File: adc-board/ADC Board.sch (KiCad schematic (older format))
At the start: 113 parts, among them J1 ST-LINK/V2, J2 Sensors, J3 USART1, J4 USART6, J5 UE27AC5410H, U1 STM32H743ZITx, U10 MCP1501T-30E/SN, U11 AP7361C-33E-13, U12 AP7361C-33E-13, U13 P78E05-1000, U3 USBLC6-2SC6, U4 AD8544, U5 AD8544, U6 AD8544, U7 AD8544, U8 AD8544, U9 AD8544, Y1 NX3225GD-8.000M-EXS00A-CG04874

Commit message: adc board schematic tweaks and complete relayout
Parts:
- removed C18, C19: 1uF, Capacitors_SMD:C_0805_HandSoldering, symbol Device:C_Small
- removed C22, C23, C24, C25: 4.7uF, Capacitors_SMD:C_0805_HandSoldering, symbol Device:C_Small
- removed C31: DC32, Capacitors_SMD:C_0805, symbol Device:C
- removed J2: Sensors, Pin_Headers:Pin_Header_Angled_2x22_Pitch2.54mm, symbol Connector_Generic:Conn_02x22_Odd_Even
- removed R1, R10, R11, R12, R13, R14, R15, R16, R17, R18, R19, R2, R20, R21, R22, R3, R4, R5, R6, R7, R8, R9: 2200, Resistors_SMD:R_0805_HandSoldering, symbol Device:R_Small_US
- removed TP1, TP10, TP11, TP12, TP13, TP14, TP15, TP16, TP17, TP18, TP19, TP2, TP20, TP21, TP22, TP3, TP4, TP5, TP6, TP7, TP8, TP9: TestPoint, Pin_Headers:Pin_Header_Straight_1x01_Pitch1.00mm, symbol Connector:TestPoint
- removed U11, U12: AP7361C-33E-13, TO_SOT_Packages_SMD:SOT-223-3_TabPin2, symbol Regulator_Linear:AP7361C-33E
- removed U4, U5, U6, U7, U8, U9: AD8544, SMD_Packages:SSOP-14, symbol AD8544:AD8544
- added C55, C56: DC, Capacitors_SMD:C_0805, symbol Device:C_Small
- C33: renamed from C16; footprint Capacitors_SMD:C_0805_HandSoldering -> Capacitors_SMD:C_0805
- C34: renamed from C3; footprint Capacitors_SMD:C_0805_HandSoldering -> Capacitors_SMD:C_0805
- C35: renamed from C4; footprint Capacitors_SMD:C_0805_HandSoldering -> Capacitors_SMD:C_0805
- C36: renamed from C5; footprint Capacitors_SMD:C_0805_HandSoldering -> Capacitors_SMD:C_0805
- C37: renamed from C6; footprint Capacitors_SMD:C_0805_HandSoldering -> Capacitors_SMD:C_0805
- C38: renamed from C7; footprint Capacitors_SMD:C_0805_HandSoldering -> Capacitors_SMD:C_0805
- C39: renamed from C8; footprint Capacitors_SMD:C_0805_HandSoldering -> Capacitors_SMD:C_0805
- C40: renamed from C9; footprint Capacitors_SMD:C_0805_HandSoldering -> Capacitors_SMD:C_0805
- C41: renamed from C10; footprint Capacitors_SMD:C_0805_HandSoldering -> Capacitors_SMD:C_0805
- C42: renamed from C11; footprint Capacitors_SMD:C_0805_HandSoldering -> Capacitors_SMD:C_0805
- C43: renamed from C12; footprint Capacitors_SMD:C_0805_HandSoldering -> Capacitors_SMD:C_0805
- C44: renamed from C13; footprint Capacitors_SMD:C_0805_HandSoldering -> Capacitors_SMD:C_0805
- C45: renamed from C14; footprint Capacitors_SMD:C_0805_HandSoldering -> Capacitors_SMD:C_0805
- C46: renamed from C15; footprint Capacitors_SMD:C_0805_HandSoldering -> Capacitors_SMD:C_0805
- C47: renamed from C1; footprint Capacitors_SMD:C_0805_HandSoldering -> Capacitors_SMD:C_0805
- C48: renamed from C2; footprint Capacitors_SMD:C_0805_HandSoldering -> Capacitors_SMD:C_0805
- C49: renamed from C29; footprint Capacitors_SMD:C_0805_HandSoldering -> Capacitors_SMD:C_0805
- C50: renamed from C30; footprint Capacitors_SMD:C_0805_HandSoldering -> Capacitors_SMD:C_0805
- C51: renamed from C20; footprint Capacitors_SMD:C_0805_HandSoldering -> Capacitors_SMD:C_0805
- C52: renamed from C21; footprint Capacitors_SMD:C_0805_HandSoldering -> Capacitors_SMD:C_0805
- R30: renamed from R29; footprint Resistors_SMD:R_0805_HandSoldering -> Resistors_SMD:R_0805
- R31: renamed from R23; footprint Resistors_SMD:R_0805_HandSoldering -> Resistors_SMD:R_0805
- R55: renamed from R25; footprint Resistors_SMD:R_0805_HandSoldering -> Resistors_SMD:R_0805
- R56: renamed from R26; footprint Resistors_SMD:R_0805_HandSoldering -> Resistors_SMD:R_0805
- R57: renamed from R27; footprint Resistors_SMD:R_0805_HandSoldering -> Resistors_SMD:R_0805
- R58: renamed from R28; footprint Resistors_SMD:R_0805_HandSoldering -> Resistors_SMD:R_0805
- U13: value P78E05-1000 -> 3.3V Reg
- renumbered C17 to C32, C26 to C53, C27 to C54, J1 to J2, U1 to U0, U3 to U9
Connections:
- net labels removed: +12V, ETH_TXD0, ETH_TXD1, ETH_TX_EN, Sen10R, Sen11R, Sen12R, Sen13R, Sen14R, Sen15R, Sen16R, Sen17R, Sen18R, Sen19R, Sen1R, Sen20R, Sen21R, Sen22R, Sen2R, Sen3R, Sen4R, Sen5R, Sen6R, Sen7R, Sen8R, Sen9R
- wire segments 487 -> 297
- no-connect marks 71 -> 76
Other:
- note removed: "Op amps taking the "raw" voltage off the sense\nresistors, and buffering it for the ADCs. Also protects\nthe ADC inputs. Op amp output voltage is limited to\nVDDA, and they're cheap/easy to replace if damaged."
- note removed: "Separate linear regulators for Digital and Analog"
- moved on the sheet: C47, C48, C49, C50, H1, H2, H3, H4, R30, TP23, TP24, TP25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

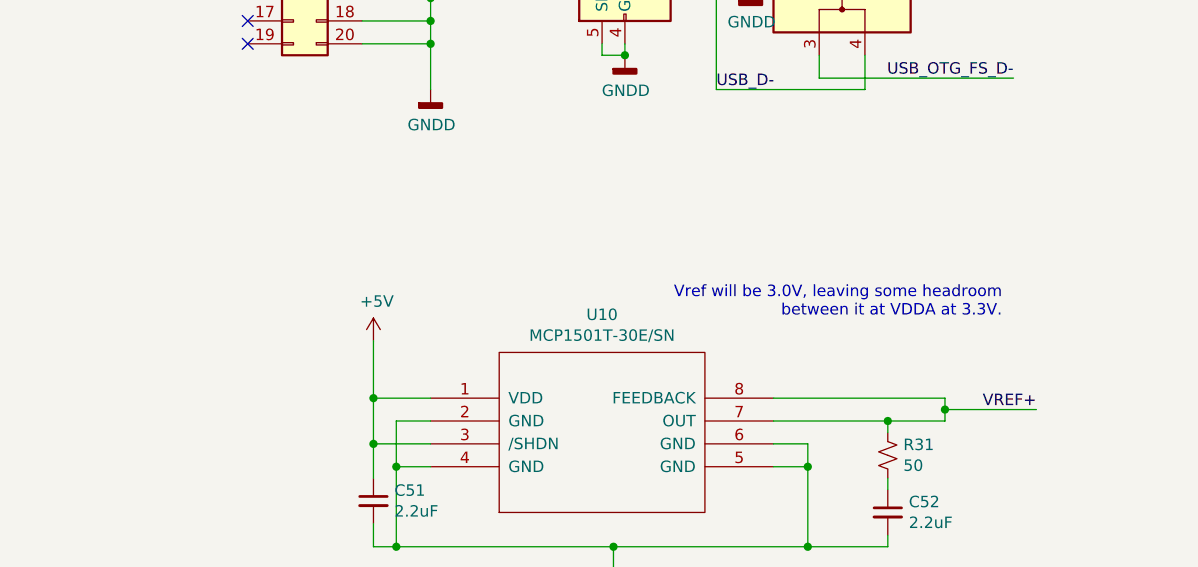
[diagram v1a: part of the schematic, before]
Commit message: correct RS485 termination resistors, adjust ground pours
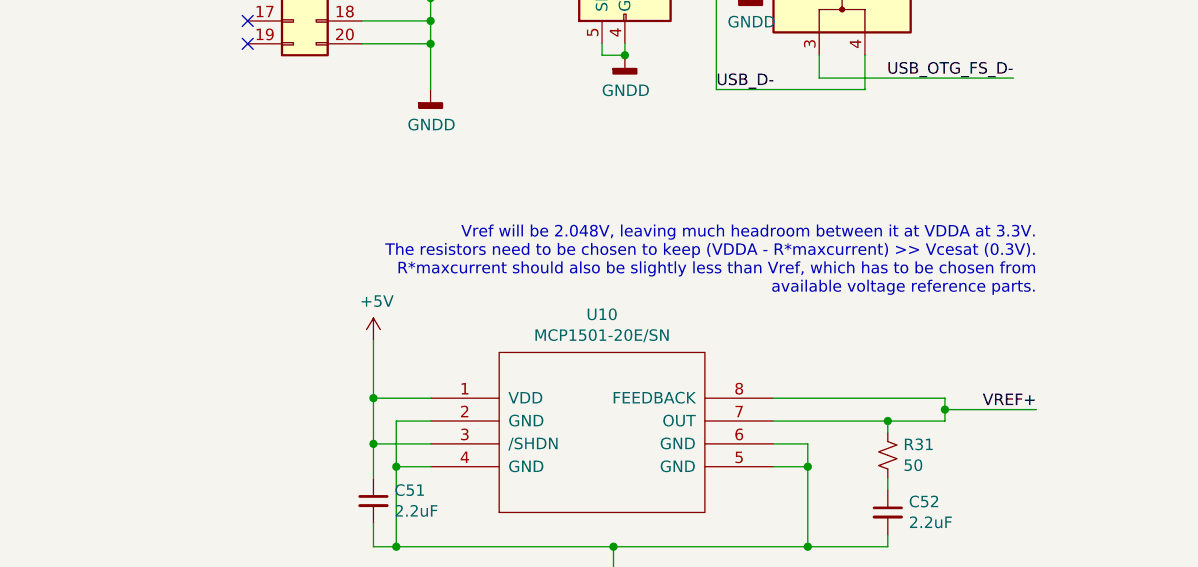
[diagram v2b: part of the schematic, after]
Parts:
- U10: value MCP1501T-30E/SN -> MCP1501-20E/SN
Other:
- note added: "Vref will be 2.048V, leaving much headroom between it at VDDA at 3.3V.\nThe resistors need to be chosen to keep (VDDA - R*maxcurrent) >> Vcesat (0.3V).\nR*maxcurrent should also be slightly less than Vref, which has to be chosen from\navailable voltage reference parts."
- note removed: "Vref will be 3.0V, leaving some headroom\nbetween it at VDDA at 3.3V."
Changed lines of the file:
@@
 P 12400 7400
 F 0 "U10" H 12400 7915 50  0000 C CNN
-F 1 "MCP1501T-30E/SN" H 12400 7824 50  0000 C CNN
+F 1 "MCP1501-20E/SN" H 12400 7824 50  0000 C CNN
 F 2 "SMD_Packages:SOIC-8-N" H 12400 7400 50  0001 C CNN
 F 3 "DOCUMENTATION" H 12400 7400 50  0001 C CNN
@@
 	1    0    0    -1
 $EndComp
-Text Notes 14150 6900 2    50   ~ 0
-Vref will be 3.0V, leaving some headroom\nbetween it at VDDA at 3.3V.
+Text Notes 14300 6800 2    50   ~ 0
+Vref will be 2.048V, leaving much headroom between it at VDDA at 3.3V.\nThe resistors need to be chosen to keep (VDDA - R*maxcurrent) >> Vcesat (0.3V).\nR*maxcurrent should also be slightly less than Vref, which has to be chosen from\navailable voltage reference parts.
 Text Notes 3600 10550 0    79   ~ 0
 Reference STMicroelectronics Application Note AN4938\nfor details on basic STMH74x circuits

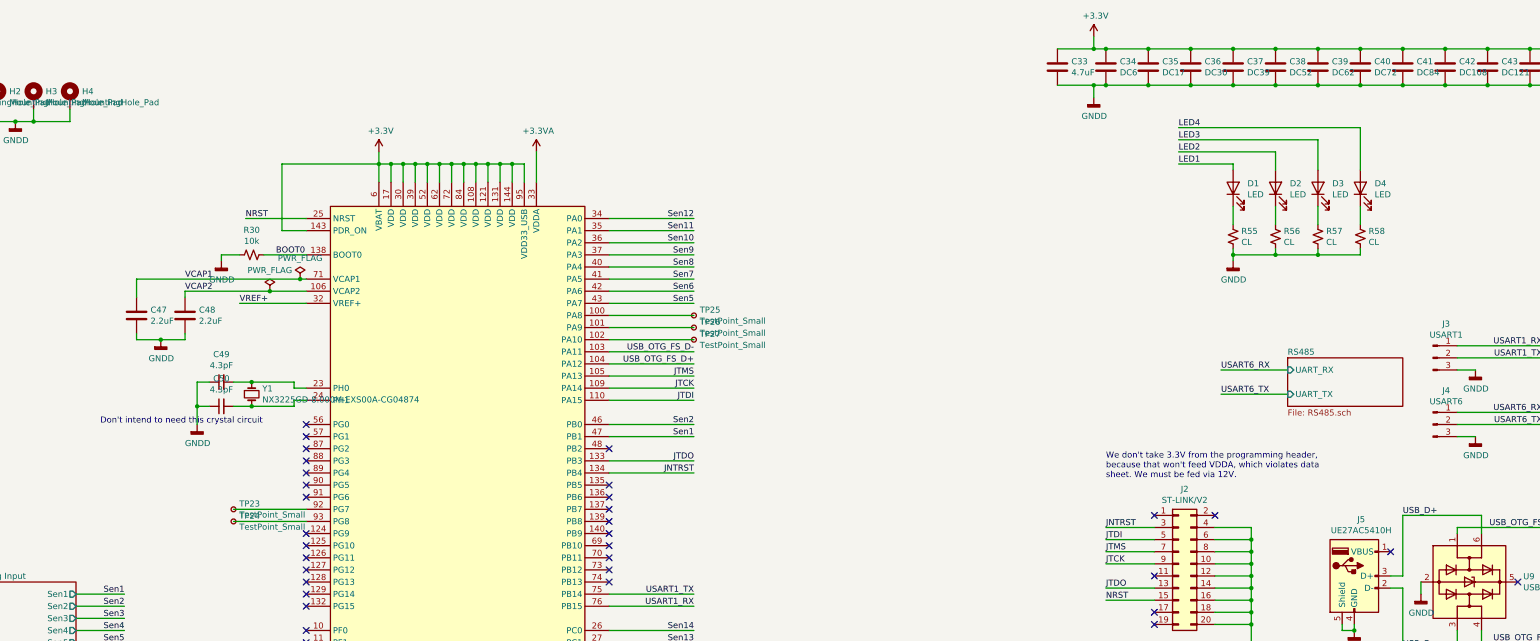
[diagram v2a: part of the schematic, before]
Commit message: alternative power inputs; cap on NRST; 3.3V reg thermal work on PCB
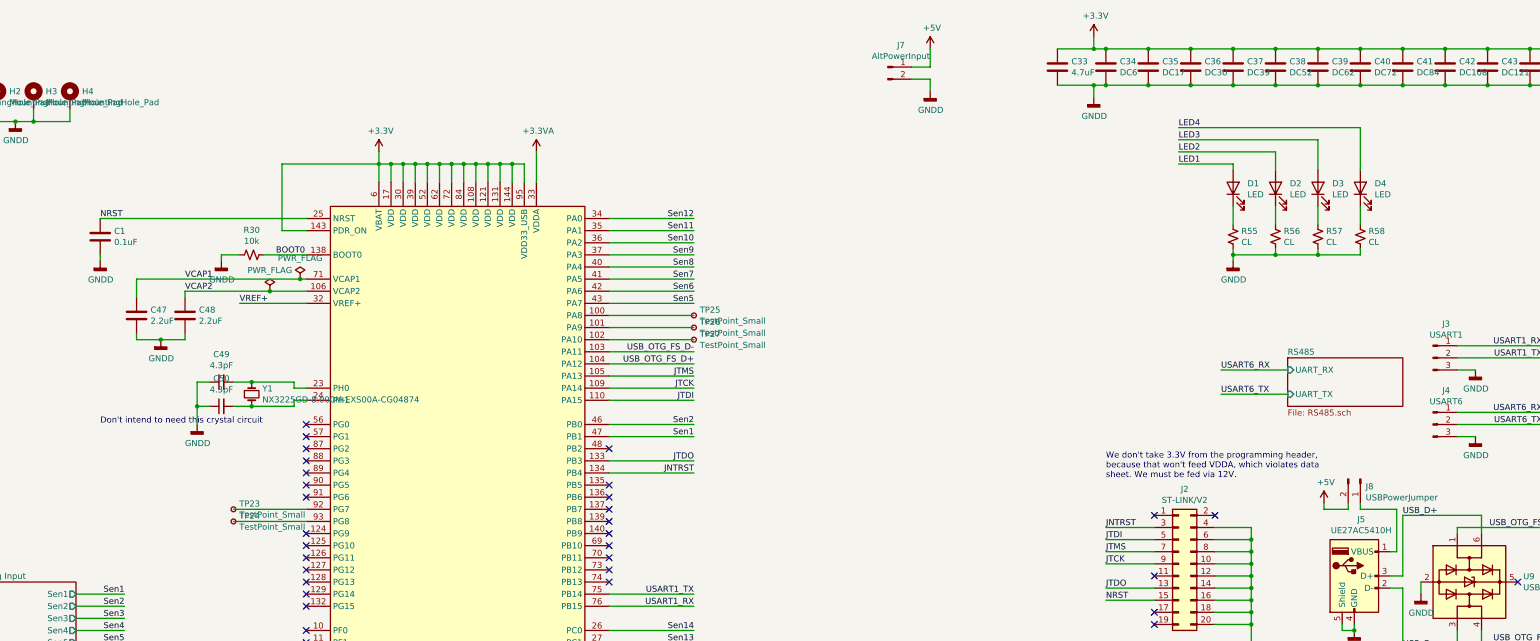
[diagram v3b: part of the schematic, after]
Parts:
- added C1: 0.1uF, Capacitors_SMD:C_0805, symbol Device:C
- added J7: AltPowerInput, Pin_Headers:Pin_Header_Straight_1x02_Pitch2.54mm, symbol Connector:Conn_01x02_Male
- added J8: USBPowerJumper, Pin_Headers:Pin_Header_Straight_1x02_Pitch2.54mm, symbol Connector:Conn_01x02_Male
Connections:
- net +5V: now also J7.1 (Pin_1), J8.2 (Pin_2)
- net GNDD: now also C1.2, J7.2 (Pin_2)
- net NRST: now also C1.1
- net at J5.1 (VBUS): now also J8.1 (Pin_1)
- no-connect marks 76 -> 75
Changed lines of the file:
@@
 NRST
 Wire Wire Line
-	3850 2350 3350 2350
-Text Label 3350 2350 0    50   ~ 0
+	3850 2350 2150 2350
+Text Label 2150 2350 0    50   ~ 0
 NRST
 Wire Wire Line
@@
 	1    0    0    -1
 $EndComp
-NoConn ~ 12800 5100
 Wire Wire Line
 	1450 1550 1600 1550
@@
 	14200 9050 14100 9050
 Connection ~ 14100 9050
+$Comp
+L Connector:Conn_01x02_Male J7
+U 1 1 5FBE56DB
+P 8650 1100
+F 0 "J7" H 8758 1281 50  0000 C CNN
+F 1 "AltPowerInput" H 8758 1190 50  0000 C CNN
+F 2 "Pin_Headers:Pin_Header_Straight_1x02_Pitch2.54mm" H 8650 1100 50  0001 C CNN
+F 3 "~" H 8650 1100 50  0001 C CNN
+	1    8650 1100
+	1    0    0    -1
+$EndComp
+$Comp
+L power:+5V #PWR0135
+U 1 1 5FBE63A7
+P 9000 950
+F 0 "#PWR0135" H 9000 800 50  0001 C CNN
+F 1 "+5V" H 9015 1123 50  0000 C CNN
+F 2 "" H 9000 950 50  0001 C CNN
+F 3 "" H 9000 950 50  0001 C CNN
+	1    9000 950
+	1    0    0    -1
+$EndComp
+Wire Wire Line
+	9000 950  9000 1100
+Wire Wire Line
+	9000 1100 8850 1100
+Wire Wire Line
+	8850 1200 9000 1200
+Wire Wire Line
+	9000 1200 9000 1300
+$Comp
+L power:GNDD #PWR0136
+U 1 1 5FC205C9
+P 9000 1300
+F 0 "#PWR0136" H 9000 1050 50  0001 C CNN
+F 1 "GNDD" H 9004 1145 50  0000 C CNN
+F 2 "" H 9000 1300 50  0001 C CNN
+F 3 "" H 9000 1300 50  0001 C CNN
+	1    9000 1300
+	1    0    0    -1
+$EndComp
+$Comp
+L Connector:Conn_01x02_Male J8
+U 1 1 5FC44C17
+P 12550 4500
+F 0 "J8" V 12612 4544 50  0000 L CNN
+F 1 "USBPowerJumper" V 12703 4544 50  0000 L CNN
+F 2 "Pin_Headers:Pin_Header_Straight_1x02_Pitch2.54mm" H 12550 4500 50  0001 C CNN
+F 3 "~" H 12550 4500 50  0001 C CNN
+	1    12550 4500
+	0    1    1    0
+$EndComp
+Wire Wire Line
+	12800 5100 12850 5100
+Wire Wire Line
+	12850 5100 12850 4750
+Wire Wire Line
+	12850 4750 12550 4750
+Wire Wire Line
+	12550 4750 12550 4700
+Wire Wire Line
+	12450 4700 12450 4750
+$Comp
+L power:+5V #PWR0143
+U 1 1 5FC885B1
+P 12250 4700
+F 0 "#PWR0143" H 12250 4550 50  0001 C CNN
+F 1 "+5V" H 12265 4873 50  0000 C CNN
+F 2 "" H 12250 4700 50  0001 C CNN
+F 3 "" H 12250 4700 50  0001 C CNN
+	1    12250 4700
+	1    0    0    -1
+$EndComp
+Wire Wire Line
+	12250 4700 12250 4750
+Wire Wire Line
+	12250 4750 12450 4750
+$Comp
+L Device:C C1
+U 1 1 5FD1E652
+P 2150 2500
+F 0 "C1" H 2265 2546 50  0000 L CNN
+F 1 "0.1uF" H 2265 2455 50  0000 L CNN
+F 2 "Capacitors_SMD:C_0805" H 2188 2350 50  0001 C CNN
+F 3 "~" H 2150 2500 50  0001 C CNN
+	1    2150 2500
+	1    0    0    -1
+$EndComp
+Wire Wire Line
+	2150 2650 2150 2700
+$Comp
+L power:GNDD #PWR0144
+U 1 1 5FD3C9A6
+P 2150 2700
+F 0 "#PWR0144" H 2150 2450 50  0001 C CNN
+F 1 "GNDD" H 2154 2545 50  0000 C CNN
+F 2 "" H 2150 2700 50  0001 C CNN
+F 3 "" H 2150 2700 50  0001 C CNN
+	1    2150 2700
+	1    0    0    -1
+$EndComp
 $EndSCHEMATC
